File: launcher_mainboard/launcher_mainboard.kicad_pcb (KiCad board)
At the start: 2 copper layers, 12 parts, among them J1 USB_B_Micro, J2 Conn_01x06, J3 Conn_01x06, J4 Conn_01x06, J5 Conn_01x06, J6 Conn_01x02, U1 ESP32-S3-MINI-1, U2 TMC2209-LA-T, U3 TMC2209-LA-T, U4 TMC2209-LA-T, U5 TMC2209-LA-T, U6 TLV75801PDRV

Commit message: ellectt elelecitfy
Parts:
- added BOOT1: SW_MEC_5E, Button_Switch_SMD:SW_MEC_5GSH9, F.Cu at (158.6, 85.8)
- added C1: 10uf, Capacitor_SMD:C_0201_0603Metric, F.Cu at (177.3, 78.3)
- added C10: 220uf, Capacitor_SMD:CP_Elec_3x5.3, F.Cu at (174.3, 109.4)
- added C11: 220uf, Capacitor_SMD:CP_Elec_3x5.3, F.Cu at (174.3, 114.3)
- added C12: 220uf, Capacitor_SMD:CP_Elec_3x5.3, F.Cu at (174.3, 119.1)
- added C15: 10uf, Capacitor_SMD:C_0201_0603Metric, F.Cu at (179.8, 78.3)
- added C16: 10uf, Capacitor_SMD:C_0201_0603Metric, F.Cu at (179.8, 80.1)
- added C2: 10uf, Capacitor_SMD:C_0201_0603Metric, F.Cu at (177.3, 80.1)
- added C3: 10uf, Capacitor_SMD:C_0201_0603Metric, F.Cu at (177.3, 81.8)
- added C4: 10uf, Capacitor_SMD:C_0201_0603Metric, F.Cu at (177.3, 83.6)
- added C5: 0.1uf, Capacitor_SMD:C_0201_0603Metric, F.Cu at (177.3, 85.3)
- added C6: 0.1uf, Capacitor_SMD:C_0201_0603Metric, F.Cu at (177.3, 87.1)
- added C7: 0.1uf, Capacitor_SMD:C_0201_0603Metric, F.Cu at (177.3, 88.8)
- added C8: 10uf, Capacitor_SMD:C_0201_0603Metric, F.Cu at (177.3, 90.6)
- added C9: 220uf, Capacitor_SMD:CP_Elec_3x5.3, F.Cu at (174.3, 104.6)
- added D1: POWER_LED, LED_SMD:LED_PLCC-2_3x2mm_AK, F.Cu at (191.4, 79.4)
- added D2: 3v, Diode_SMD:D_0201_0603Metric, F.Cu at (187.5, 115.5)
- added D3: D_Schottky, Diode_SMD:D_0201_0603Metric, F.Cu at (187.5, 117.2)
- added D4: INDICATOR_LED_1, LED_SMD:LED_PLCC-2_3x2mm_AK, F.Cu at (191.4, 83.3)
- added D5: INDICATOR_LED_2, LED_SMD:LED_PLCC-2_3x2mm_AK, F.Cu at (191.4, 87.2)
- added D6: D_Schottky, Diode_SMD:D_0201_0603Metric, F.Cu at (187.5, 119.0)
- added F1: Fuse, Fuse:FuseHolder_Blade_ATO_Littelfuse_FLR_178.6165, F.Cu at (162.3, 96.9)
- added J10: pin headers, Connector_PinHeader_2.54mm:PinHeader_1x14_P2.54mm_Vertical, F.Cu at (150.5, 79.8)
- added J7: fan_con, Connector_Molex:Molex_PicoBlade_53047-0210_1x02_P1.25mm_Vertical, F.Cu at (182.3, 117.7)
- added J8: ESC_1, Connector_AMASS:AMASS_XT60-F_1x02_P7.20mm_Vertical, F.Cu at (184.9, 99.2)
- added J9: ESC_2, Connector_AMASS:AMASS_XT60-F_1x02_P7.20mm_Vertical, F.Cu at (184.9, 109.5)
- added Q1: 2N7002H, Package_TO_SOT_SMD:SOT-23, F.Cu at (155.3, 96.5)
- added Q2: 2N3904, Package_TO_SOT_THT:TO-92_Inline, F.Cu at (196.4, 80.7)
- added Q3: 2N3904, Package_TO_SOT_THT:TO-92_Inline, F.Cu at (196.4, 86.5)
- added Q4: BSS138, Package_TO_SOT_SMD:SOT-23, F.Cu at (155.3, 101.1)
- added Q5: BSS138, Package_TO_SOT_SMD:SOT-23, F.Cu at (155.3, 105.8)
- added Q6: BSS138, Package_TO_SOT_SMD:SOT-23, F.Cu at (155.3, 110.4)
- added Q7: BSS138, Package_TO_SOT_SMD:SOT-23, F.Cu at (155.3, 115.0)
- added Q8: PMOS, Package_DFN_QFN:DFN-6-1EP_2x1.6mm_P0.5mm_EP1.15x1.3mm, F.Cu at (196.3, 116.3)
- added R1: 1M, Resistor_SMD:R_0201_0603Metric, F.Cu at (179.8, 81.8)
- added R10: 200, Resistor_SMD:R_0201_0603Metric, F.Cu at (182.2, 83.6)
- added R11: 20k, Resistor_SMD:R_0201_0603Metric, F.Cu at (182.2, 85.3)
- added R12: 200, Resistor_SMD:R_0201_0603Metric, F.Cu at (182.2, 87.1)
- added R13: 20k, Resistor_SMD:R_0201_0603Metric, F.Cu at (182.2, 88.8)
- added R14: 10k, Resistor_SMD:R_0201_0603Metric, F.Cu at (182.2, 90.6)
- added R15: 10k, Resistor_SMD:R_0201_0603Metric, F.Cu at (184.7, 78.3)
- added R16: 10k, Resistor_SMD:R_0201_0603Metric, F.Cu at (184.7, 80.1)
- added R17: 10k, Resistor_SMD:R_0201_0603Metric, F.Cu at (184.7, 81.8)
- added R18: 10k, Resistor_SMD:R_0201_0603Metric, F.Cu at (184.7, 83.6)
- added R19: 10k, Resistor_SMD:R_0201_0603Metric, F.Cu at (184.7, 85.3)
- added R2: 200k, Resistor_SMD:R_0201_0603Metric, F.Cu at (179.8, 83.6)
- added R20: 10k, Resistor_SMD:R_0201_0603Metric, F.Cu at (184.7, 87.1)
- added R21: 10k, Resistor_SMD:R_0201_0603Metric, F.Cu at (184.7, 88.8)
- added R22: 50k, Resistor_SMD:R_0201_0603Metric, F.Cu at (184.7, 90.6)
- added R23: 75k, Resistor_SMD:R_0201_0603Metric, F.Cu at (187.1, 78.3)
- added R24: 50k, Resistor_SMD:R_0201_0603Metric, F.Cu at (187.1, 80.1)
- added R25: 75k, Resistor_SMD:R_0201_0603Metric, F.Cu at (187.1, 81.8)
- added R26: 50k, Resistor_SMD:R_0201_0603Metric, F.Cu at (187.1, 83.6)
- added R27: 75k, Resistor_SMD:R_0201_0603Metric, F.Cu at (187.1, 85.3)
- added R28: 50k, Resistor_SMD:R_0201_0603Metric, F.Cu at (187.1, 87.1)
- added R29: 75k, Resistor_SMD:R_0201_0603Metric, F.Cu at (187.1, 88.8)
- added R3: 200, Resistor_SMD:R_0201_0603Metric, F.Cu at (179.8, 85.3)
- added R4: 10k, Resistor_SMD:R_0201_0603Metric, F.Cu at (179.8, 87.1)
- added R5: 10k, Resistor_SMD:R_0201_0603Metric, F.Cu at (179.8, 88.8)
- added R6: 50k, Resistor_SMD:R_0201_0603Metric, F.Cu at (179.8, 90.6)
- added R7: 4k, Resistor_SMD:R_0201_0603Metric, F.Cu at (182.2, 78.3)
- added R8: ?, Resistor_SMD:R_0201_0603Metric, F.Cu at (182.2, 80.1)
- added R9: ?, Resistor_SMD:R_0201_0603Metric, F.Cu at (182.2, 81.8)
- added RESET1: SW_MEC_5E, Button_Switch_SMD:SW_MEC_5GSH9, F.Cu at (170.3, 85.8)
- added U10: MAX40200AUK, Package_TO_SOT_SMD:SOT-23-5, F.Cu at (191.3, 117.0)
- added U7: R-78E3.3-0.5, Converter_DCDC:Converter_DCDC_RECOM_R-78E-0.5_THT, F.Cu at (161.9, 109.4)
- added U8: D3V3XA4B10LP, Package_DFN_QFN:Diodes_UDFN-10_1.0x2.5mm_P0.5mm, F.Cu at (195.6, 120.0)
- added U9: R-78E5.0-0.5, Converter_DCDC:Converter_DCDC_RECOM_R-78E-0.5_THT, F.Cu at (161.9, 119.6)
- J6: value Conn_01x02 -> bat_con
- U2: footprint TMC2209-LA-T:QFN28_5X5_3X8_EPAD_TRI -> CustomFootprints:TCM2209_Module
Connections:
- J1 pad 1: unconnected-(J1-VBUS-Pad1) -> /+5VUSB
- J1 pad 2: unconnected-(J1-D--Pad2) -> /USB_D-
- J1 pad 3: unconnected-(J1-D+-Pad3) -> /USB_D+
- J1 pad 5: GND -> -BATT
- J1 pad 6: GND -> -BATT
- J6 pad 1: unconnected-(J6-Pin_1-Pad1) -> -BATT
- J6 pad 2: unconnected-(J6-Pin_2-Pad2) -> Net-(J6-Pin_2)
- U1 pad 1: GND -> -BATT
- U1 pad 14: unconnected-(U1-IO10-Pad14) -> /ind_LED_1
- U1 pad 15: unconnected-(U1-IO11-Pad15) -> /ind_LED_2
- U1 pad 2: GND -> -BATT
- U1 pad 3: unconnected-(U1-3V3-Pad3) -> +3.3V
- U1 pad 4: /motor_en -> Net-(BOOT1-A)
- U1 pad 41: unconnected-(U1-IO45-Pad41) -> /PDN_UART_TX
- U1 pad 42: GND -> -BATT
- U1 pad 43: GND -> -BATT
- U1 pad 44: unconnected-(U1-IO46-Pad44) -> /PDN_UART_RX
- U1 pad 45: unconnected-(U1-EN-Pad45) -> Net-(RESET1-A)
- U1 pad 46: GND -> -BATT
- U1 pad 47: GND -> -BATT
- U1 pad 48: GND -> -BATT
- U1 pad 49: GND -> -BATT
- U1 pad 5: unconnected-(U1-IO1-Pad5) -> /motor_en
- U1 pad 50: GND -> -BATT
- U1 pad 51: GND -> -BATT
- U1 pad 52: GND -> -BATT
- U1 pad 53: GND -> -BATT
- U1 pad 54: GND -> -BATT
- U1 pad 55: GND -> -BATT
- U1 pad 56: GND -> -BATT
- U1 pad 57: GND -> -BATT
- U1 pad 58: GND -> -BATT
- U1 pad 59: GND -> -BATT
- U1 pad 60: GND -> -BATT
- U1 pad 61: GND -> -BATT
- U1 pad 62: GND -> -BATT
- U1 pad 63: GND -> -BATT
- U1 pad 64: GND -> -BATT
- U1 pad 65: GND -> -BATT
- U3 pad 14: unconnected-(U3-PDN_UART-Pad14) -> /PDN_UART_RX
- U3 pad 16: unconnected-(U3-STEP-Pad16) -> /M2_STEP
- U3 pad 18: GND -> -BATT
- U3 pad 19: unconnected-(U3-DIR-Pad19) -> /M2_DIR
- U3 pad 22: unconnected-(U3-VS-Pad22) -> +BATT
- U3 pad 28: unconnected-(U3-VS-Pad28) -> +BATT
- U3 pad 29: GND -> -BATT
- U3 pad 3: GND -> -BATT
- U3 pad 9: GND -> -BATT
- U4 pad 10: GND -> -BATT
- U4 pad 14: unconnected-(U4-PDN_UART-Pad14) -> /PDN_UART_RX
- U4 pad 16: unconnected-(U4-STEP-Pad16) -> /M3_STEP
- U4 pad 18: GND -> -BATT
- U4 pad 19: unconnected-(U4-DIR-Pad19) -> /M3_DIR
- U4 pad 22: unconnected-(U4-VS-Pad22) -> +BATT
- U4 pad 28: unconnected-(U4-VS-Pad28) -> +BATT
- U4 pad 29: GND -> -BATT
- U4 pad 3: GND -> -BATT
- U5 pad 14: unconnected-(U5-PDN_UART-Pad14) -> /PDN_UART_RX
- U5 pad 16: unconnected-(U5-STEP-Pad16) -> /M4_STEP
- U5 pad 18: GND -> -BATT
- U5 pad 19: unconnected-(U5-DIR-Pad19) -> /M4_DIR
- U5 pad 22: unconnected-(U5-VS-Pad22) -> +BATT
- U5 pad 28: unconnected-(U5-VS-Pad28) -> +BATT
- U5 pad 29: GND -> -BATT
- U5 pad 3: GND -> -BATT
- U6 pad 1: unconnected-(U6-OUT-Pad1) -> /3.5VUSB
- U6 pad 2: unconnected-(U6-FB-Pad2) -> Net-(U6-FB)
- U6 pad 3: Net-(U6-GND-Pad3) -> -BATT
- U6 pad 4: unconnected-(U6-EN-Pad4) -> /+5VUSB
- U6 pad 6: unconnected-(U6-IN-Pad6) -> /+5VUSB
- U6 pad 7: Net-(U6-GND-Pad3) -> -BATT

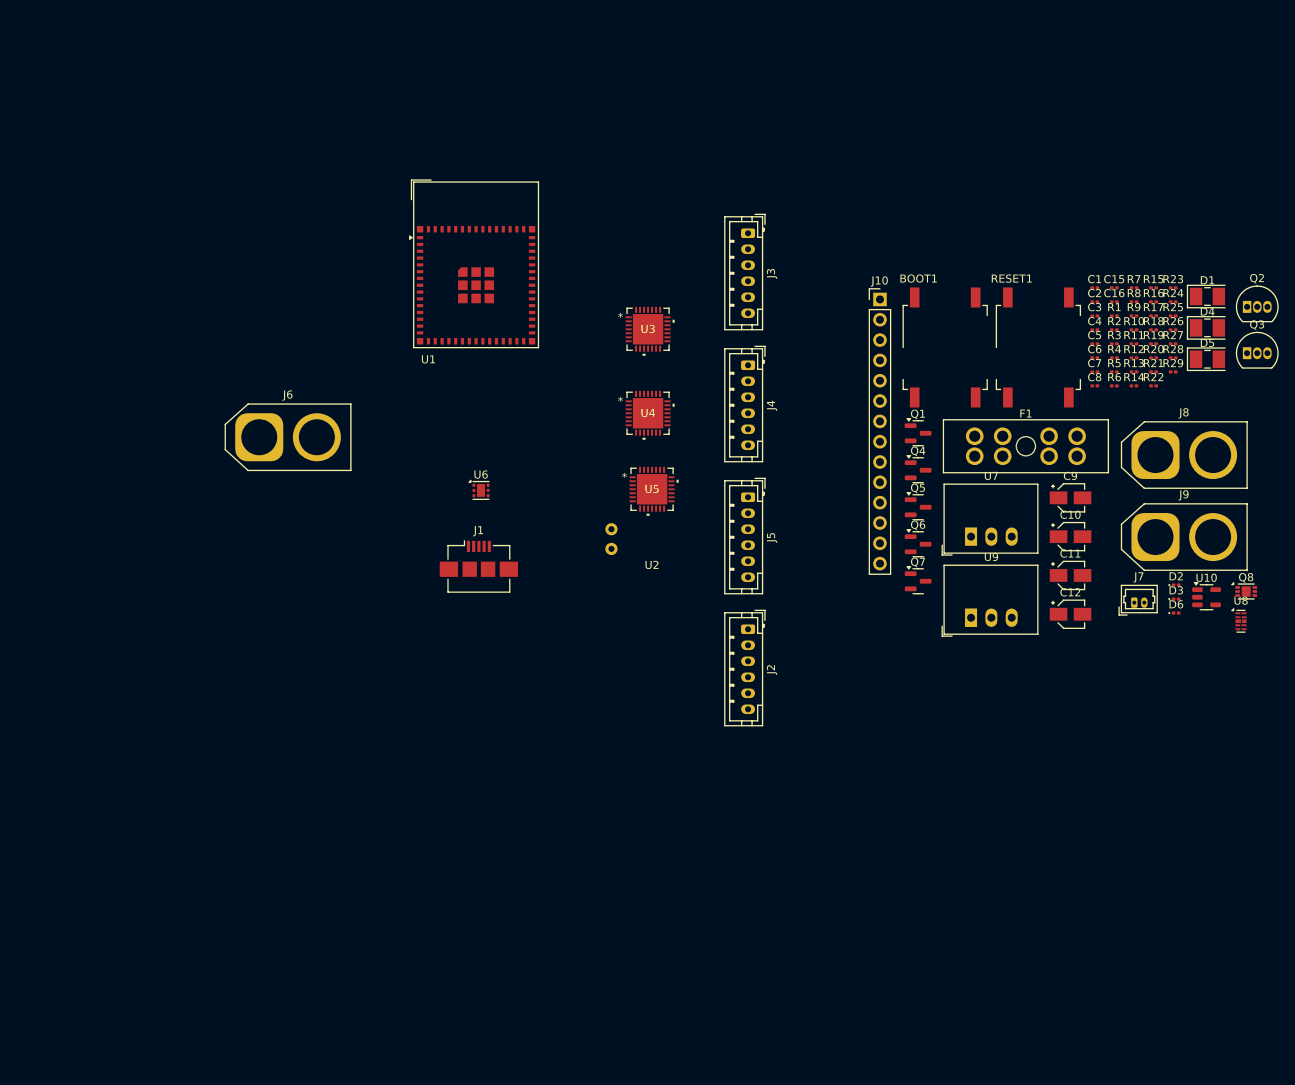
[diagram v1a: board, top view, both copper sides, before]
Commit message: first complete scematic draft
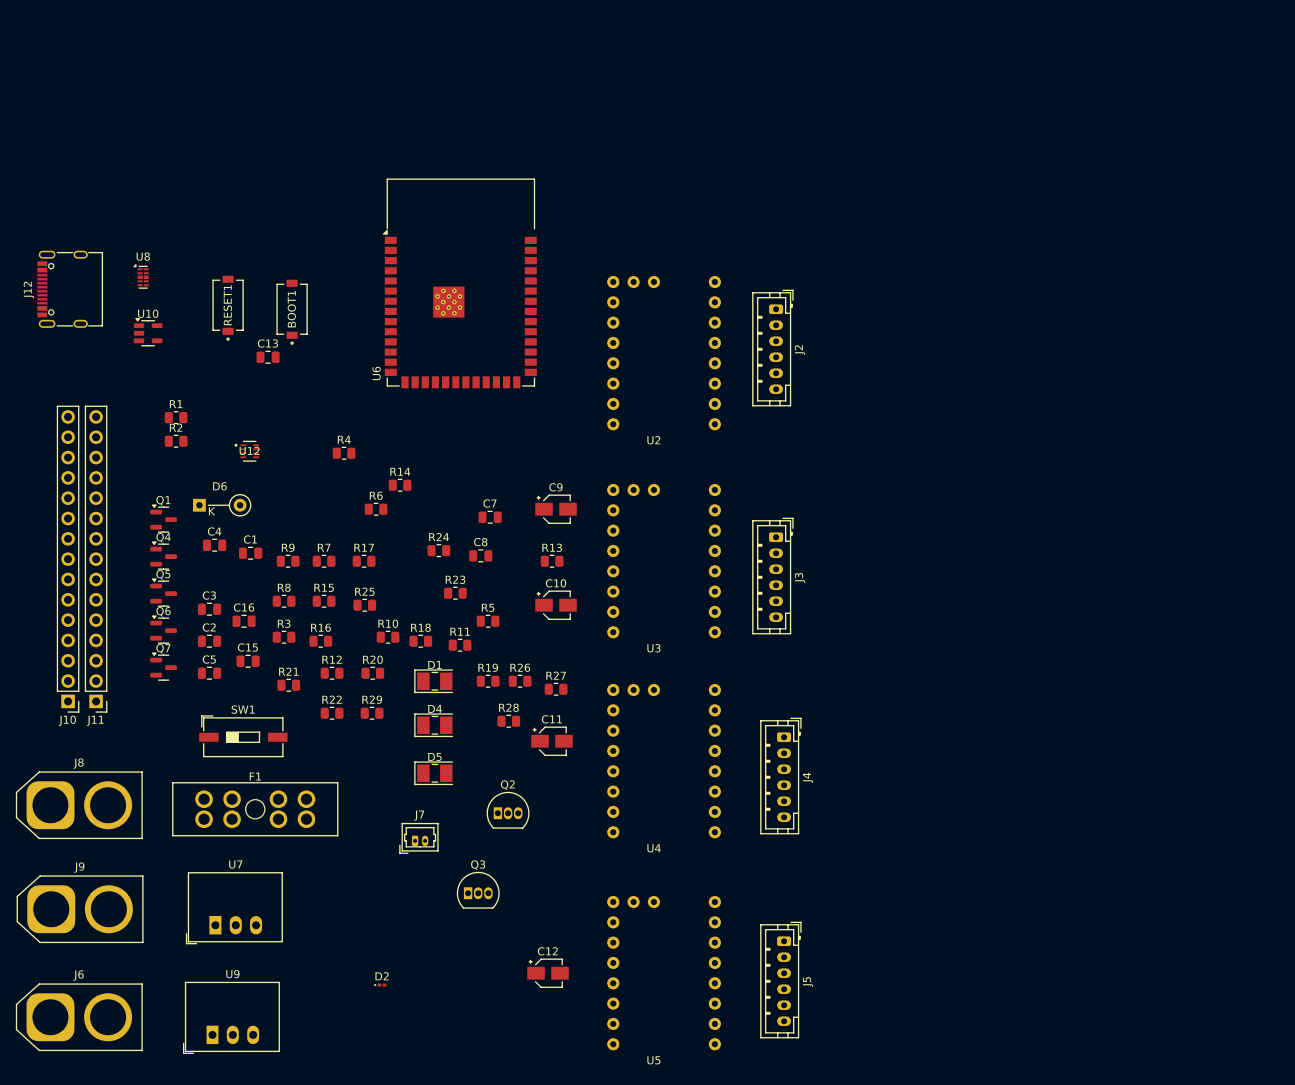
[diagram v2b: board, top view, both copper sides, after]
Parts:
- removed C6: 0.1uf, Capacitor_SMD:C_0201_0603Metric
- removed D3: D_Schottky, Diode_SMD:D_0201_0603Metric
- removed J1: USB_B_Micro, Connector_USB:USB_Micro-B_Amphenol_10104110_Horizontal
- removed Q8: PMOS, Package_DFN_QFN:DFN-6-1EP_2x1.6mm_P0.5mm_EP1.15x1.3mm
- removed U1: ESP32-S3-MINI-1, RF_Module:ESP32-S2-MINI-1
- added C13: 4.7uf, Capacitor_SMD:C_0805_2012Metric, F.Cu at (74.0, 87.0)
- added J11: header, Connector_PinHeader_2.54mm:PinHeader_1x15_P2.54mm_Vertical, F.Cu at (52.5, 130.0)
- added J12: USB_C_Receptacle_USB2.0_16P, Connector_USB:USB_C_Receptacle_G-Switch_GT-USB-7010ASV, F.Cu at (49.5, 78.5)
- added SW1: POWER_SWITCH, Button_Switch_SMD:SW_DIP_SPSTx01_Slide_9.78x4.72mm_W8.61mm_P2.54mm, F.Cu at (70.9, 134.5)
- added U12: LM66200DRLR, LM66200:SOT-5X3_DRL_TEX, F.Cu at (71.7, 98.7)
- BOOT1, RESET1: value SW_MEC_5E -> PTS636 SM43 SMTR LFS; footprint Button_Switch_SMD:SW_MEC_5GSH9 -> PTS636:SW_PTS636_CNK
- C1, C15, C16, C2, C3, C4, C7, C8: footprint Capacitor_SMD:C_0201_0603Metric -> Capacitor_SMD:C_0805_2012Metric
- C5: value 0.1uf -> 1uf; footprint Capacitor_SMD:C_0201_0603Metric -> Capacitor_SMD:C_0805_2012Metric
- D6: value D_Schottky -> 1N4004; footprint Diode_SMD:D_0201_0603Metric -> Diode_THT:D_DO-35_SOD27_P5.08mm_Vertical_KathodeUp
- J10: value pin headers -> header; footprint Connector_PinHeader_2.54mm:PinHeader_1x14_P2.54mm_Vertical -> Connector_PinHeader_2.54mm:PinHeader_1x15_P2.54mm_Vertical
- R1: value 1M -> 5.1k; footprint Resistor_SMD:R_0201_0603Metric -> Resistor_SMD:R_0805_2012Metric
- R10, R12, R14, R15, R16, R17, R18, R19, R20, R21, R22, R23, R24, R25, R26, R27, R28, R29, R3, R4, R6, R7: footprint Resistor_SMD:R_0201_0603Metric -> Resistor_SMD:R_0805_2012Metric
- R11, R13: value 20k -> 10k; footprint Resistor_SMD:R_0201_0603Metric -> Resistor_SMD:R_0805_2012Metric
- R2: value 200k -> 5.1k; footprint Resistor_SMD:R_0201_0603Metric -> Resistor_SMD:R_0805_2012Metric
- R5: value 10k -> 1k; footprint Resistor_SMD:R_0201_0603Metric -> Resistor_SMD:R_0805_2012Metric
- R8: value ? -> 10k; footprint Resistor_SMD:R_0201_0603Metric -> Resistor_SMD:R_0805_2012Metric
- R9: value ? -> 1.5k; footprint Resistor_SMD:R_0201_0603Metric -> Resistor_SMD:R_0805_2012Metric
- U10: value MAX40200AUK -> TLV75533PDBV
- U3, U4, U5: footprint TMC2209-LA-T:QFN28_5X5_3X8_EPAD_TRI -> CustomFootprints:TCM2209_Module
- U6: value TLV75801PDRV -> ESP32-S3-WROOM-1; footprint Package_SON:WSON-6-1EP_2x2mm_P0.65mm_EP1x1.6mm -> RF_Module:ESP32-S3-WROOM-1
- moved J9 145.7 mm to (46.9, 156.0)
- moved J8 144.9 mm to (46.8, 143.0)
- moved U8 143.8 mm to (58.4, 77.0)
- moved U10 136.4 mm to (59.0, 84.0)
- moved D6 122.8 mm to (65.4, 105.5)
- moved C2 118.5 mm to (66.7, 122.5)
- moved Q3 118.5 mm to (99.0, 154.0)
- moved R2 118.1 mm to (62.5, 97.5)
- moved C5 118.1 mm to (66.7, 126.5)
- moved R1 118.0 mm to (62.5, 94.5)
- moved C15 117.9 mm to (71.5, 125.0)
- moved C3 116.6 mm to (66.7, 118.5)
- moved C16 115.9 mm to (71.0, 120.0)
- moved R21 115.0 mm to (76.6, 128.0)
- moved C4 113.3 mm to (67.3, 110.5)
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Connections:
- BOOT1 pad 2: -BATT -> Net-(U6-IO0)
- C4 pad 1: /3.5VUSB -> /3.3VUSB
- C5 pad 1: Net-(RESET1-A) -> Net-(U6-EN)
- D6 pad 1: +3.3V -> +BATT
- D6 pad 2: /3.5VUSB -> Net-(D6-A)
- F1 pad 1: Net-(J6-Pin_2) -> Net-(F1-Pad1)
- J10 pad 1: unconnected-(J10-Pin_1-Pad1) -> -BATT
- J10 pad 10: unconnected-(J10-Pin_10-Pad10) -> /HV_SIGNAL_1
- J10 pad 11: unconnected-(J10-Pin_11-Pad11) -> /HV_SIGNAL_3
- J10 pad 12: unconnected-(J10-Pin_12-Pad12) -> /IO_EXTRA_1
- J10 pad 13: unconnected-(J10-Pin_13-Pad13) -> /IO_EXTRA_3
- J10 pad 14: unconnected-(J10-Pin_14-Pad14) -> /IO_EXTRA_5
- J10 pad 2: unconnected-(J10-Pin_2-Pad2) -> -BATT
- J10 pad 3: unconnected-(J10-Pin_3-Pad3) -> -BATT
- J10 pad 4: unconnected-(J10-Pin_4-Pad4) -> +5V
- J10 pad 5: unconnected-(J10-Pin_5-Pad5) -> +5V
- J10 pad 6: unconnected-(J10-Pin_6-Pad6) -> +5V
- J10 pad 7: unconnected-(J10-Pin_7-Pad7) -> +3.3V
- J10 pad 8: unconnected-(J10-Pin_8-Pad8) -> /HV1
- J10 pad 9: unconnected-(J10-Pin_9-Pad9) -> /HV3
- J7 pad 2: Net-(D3-A) -> Net-(D6-A)
- Q1 pad 3: Net-(D3-A) -> Net-(D6-A)
- R1 pad 1: /3.5VUSB -> -BATT
- R1 pad 2: Net-(U6-FB) -> Net-(J12-CC1)
- R2 pad 1: Net-(U6-FB) -> -BATT
- R2 pad 2: -BATT -> Net-(J12-CC2)
- R3 pad 2: /3.5VUSB -> /3.3VUSB
- R4 pad 1: Net-(RESET1-A) -> Net-(U6-EN)
- R5 pad 1: /PDN_UART_RX -> Net-(U6-IO2)
- R5 pad 2: /PDN_UART_TX -> /PDN_UART
- RESET1 pad 2: -BATT -> Net-(U6-EN)
- U10 pad 1: /+3.3VBatt -> /+5VUSB
- U10 pad 3: Net-(Q8-D) -> /+5VUSB
- U10 pad 5: +3.3V -> /3.3VUSB
- U3 pad 14: /PDN_UART_RX -> /PDN_UART
- U4 pad 14: /PDN_UART_RX -> /PDN_UART
- U5 pad 14: /PDN_UART_RX -> /PDN_UART
- U6 pad 1: /3.5VUSB -> -BATT
- U6 pad 2: Net-(U6-FB) -> +3.3V
- U6 pad 3: -BATT -> Net-(U6-EN)
- U6 pad 4: /+5VUSB -> /IO_EXTRA_6
- U6 pad 5: unconnected-(U6-DNC-Pad5) -> /IO_EXTRA_5
- U6 pad 6: /+5VUSB -> /IO_EXTRA_4
- U6 pad 7: -BATT -> /IO_EXTRA_3
- U8 pad 1: /USB_D- -> /USB_D+
- U8 pad 2: /USB_D+ -> /USB_D-

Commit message: added more footprints. Rought layout
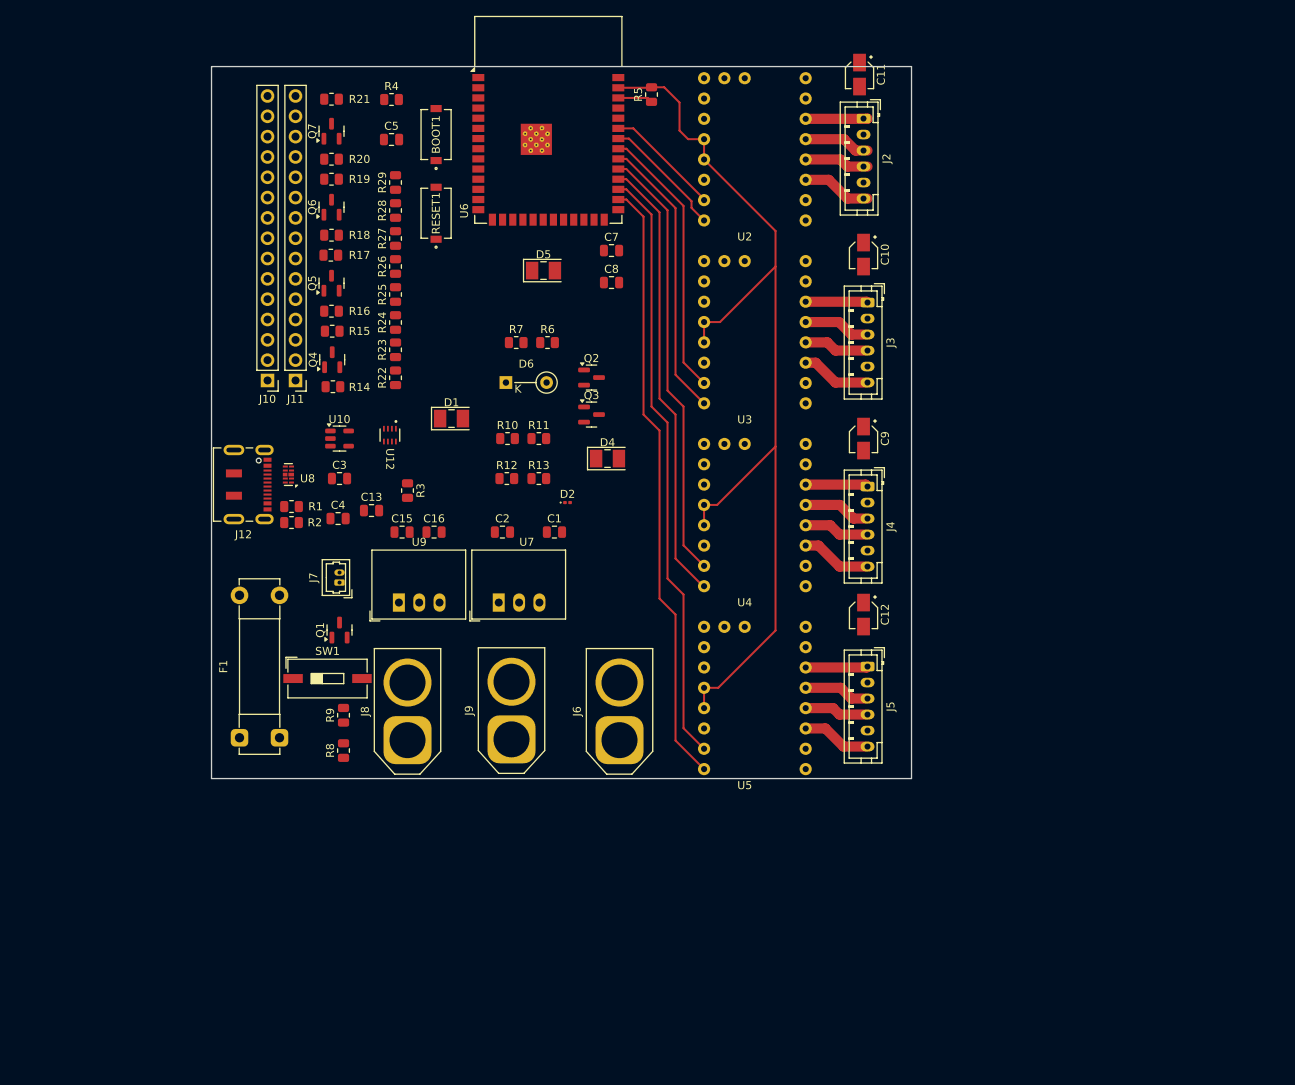
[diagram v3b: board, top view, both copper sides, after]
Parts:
- F1: footprint Fuse:FuseHolder_Blade_ATO_Littelfuse_FLR_178.6165 -> Fuse:Fuseholder_Clip-5x20mm_Bel_FC-203-22_Lateral_P17.80x5.00mm_D1.17mm_Horizontal
- J12: footprint Connector_USB:USB_C_Receptacle_G-Switch_GT-USB-7010ASV -> Connector_USB:USB_C_Receptacle_JAE_DX07S016JA1R1500
- Q2, Q3: value 2N3904 -> MMBT3904; footprint Package_TO_SOT_THT:TO-92_Inline -> Package_TO_SOT_SMD:SOT-23
- moved C11 91.8 mm to (147.9, 51.7), turned to -90 degrees
- moved J6 79.1 mm to (117.9, 134.9), turned to 90 degrees
- moved R21 73.5 mm to (81.9, 54.7), turned to 180 degrees
- moved C5 70.5 mm to (89.4, 59.8)
- moved Q7 70.3 mm to (81.9, 58.7), turned to 90 degrees
- moved R5 68.9 mm to (121.9, 54.2), turned to 90 degrees
- moved R29 66.4 mm to (89.9, 65.2), turned to 90 degrees
- moved R19 65.7 mm to (81.9, 64.7), turned to 180 degrees
- moved R28 65.4 mm to (89.9, 68.7), turned to 90 degrees
- moved D2 64.6 mm to (111.4, 105.2)
- moved R20 64.5 mm to (81.9, 62.2), turned to 180 degrees
- moved D5 64.3 mm to (108.4, 76.2)
- moved Q3 61.8 mm to (114.4, 94.2)
- moved J9 61.3 mm to (104.4, 134.8), turned to 90 degrees
- moved R27 59.8 mm to (89.9, 72.2), turned to 90 degrees
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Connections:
- Q2 pad 1: -BATT -> Net-(Q2-B)
- Q2 pad 2: Net-(Q2-B) -> -BATT
- Q3 pad 1: -BATT -> Net-(Q3-B)
- Q3 pad 2: Net-(Q3-B) -> -BATT
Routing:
- net /PDN_UART: track 0.00 -> 123.9 mm
- net /M4_DIR: track 0.00 -> 76.2 mm
- net /M4_STEP: track 0.00 -> 75.0 mm
- net /M3_DIR: track 0.00 -> 56.0 mm
- net /M3_STEP: track 0.00 -> 54.6 mm
- net /M2_DIR: track 0.00 -> 35.6 mm
- net /M2_STEP: track 0.00 -> 34.3 mm
- net /M1_DIR: track 0.00 -> 15.5 mm
- net /M1_STEP: track 0.00 -> 14.5 mm
- net /M3_B2: track 0.00 -> 8.82 mm
- net /M2_B2: track 0.00 -> 8.76 mm
- net /M1_B2: track 0.00 -> 8.70 mm
- net /M4_B2: track 0.00 -> 8.67 mm
- net /M3_A1: track 0.00 -> 8.44 mm
- net /M2_A1: track 0.00 -> 8.38 mm
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- added copper zone on In2.Cu, net +3.3V
- added copper zone on In2.Cu, net +BATT
- added copper zone on In1.Cu, net -BATT
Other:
- board outline added: 87.5 x 89 mm
- copper layers 2 -> 4
